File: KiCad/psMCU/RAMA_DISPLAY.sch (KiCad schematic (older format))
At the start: 7 parts

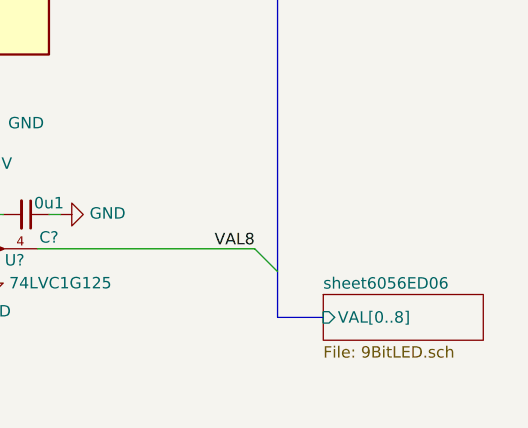
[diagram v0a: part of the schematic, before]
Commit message: Started ClockTest PCB
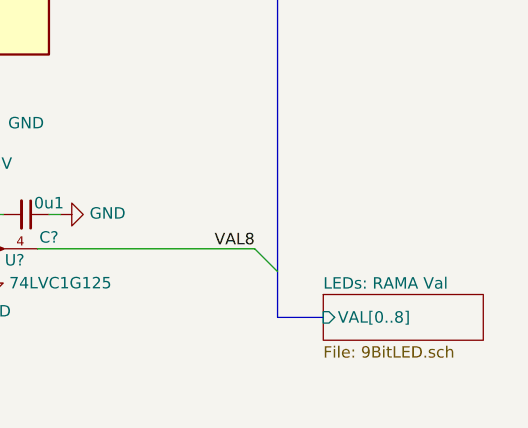
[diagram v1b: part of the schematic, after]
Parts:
- removed C?: 0u1, Capacitor_SMD:C_0603_1608Metric, symbol Device:C_Small
- removed R?: 10K, Resistor_SMD:R_0603_1608Metric, symbol Device:R_Small
- removed U?: 74HC245, symbol 74xx:74HC245
- removed U?: 74LVC1G04, Package_TO_SOT_SMD:SOT-353_SC-70-5, symbol 74xGxx:74LVC1G04
- added C?: 0u1, Capacitor_SMD:C_0603_1608Metric, symbol Device:C_Small
- added R?: 10K, Resistor_SMD:R_0603_1608Metric, symbol Device:R_Small
- added U?: 74HC245, symbol 74xx:74HC245
- added U?: 74LVC1G04, Package_TO_SOT_SMD:SOT-353_SC-70-5, symbol 74xGxx:74LVC1G04
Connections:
- net +5V: now also C?.2, U?.1 (A->B), U?.20 (VCC), U?.5 (VCC)
- net GND: now also C?.1, R?.2, U?.10 (GND), U?.3 (GND)
- net RAMA0: now also U?.2 (A0)
- net RAMA1: now also U?.3 (A1)
- net RAMA2: now also U?.4 (A2)
- net RAMA3: now also U?.5 (A3)
- net RAMA4: now also U?.6 (A4)
- net RAMA5: now also U?.7 (A5)
- net RAMA6: now also U?.8 (A6)
- net RAMA7: now also U?.9 (A7)
- net RAMA_OUT: now also R?.1, U?.2
- net VAL0: now also U?.18 (B0)
- net VAL1: now also U?.17 (B1)
- net VAL2: now also U?.16 (B2)
- net VAL3: now also U?.15 (B3)
- net VAL4: now also U?.14 (B4)
- net VAL5: now also U?.13 (B5)
- net VAL6: now also U?.12 (B6)
- net VAL7: now also U?.11 (B7)
- net at U?.1: now also U?.19 (CE), U?.4
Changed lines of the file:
@@
 $Descr A4 11693 8268
 encoding utf-8
-Sheet 79 94
-Title ""
+Sheet 77 193
+Title "psMCU"
 Date ""
 Rev ""
-Comp ""
+Comp "Philipp Schilk"
 Comment1 ""
 Comment2 ""
@@
 $Comp
 L 74xx:74HC245 U?
-U 1 1 5F40D07B
+U 1 1 5FDB352A
 P 5400 1900
-AR Path="/5ED2705B/5F40D07B" Ref="U?"  Part="1"
-AR Path="/5F1CE57C/5F40D07B" Ref="U?"  Part="1"
-AR Path="/5F396002/5F40D07B" Ref="U?"  Part="1"
-AR Path="/5F394B96/5F40D07B" Ref="U?"  Part="1"
-AR Path="/6041A022/5F40D07B" Ref="U?"  Part="1"
-AR Path="/604F08FB/5F40D07B" Ref="U?"  Part="1"
+AR Path="/5ED2705B/5FDB352A" Ref="U?"  Part="1"
+AR Path="/5F1CE57C/5FDB352A" Ref="U?"  Part="1"
+AR Path="/5F396002/5FDB352A" Ref="U?"  Part="1"
+AR Path="/5F394B96/5FDB352A" Ref="U?"  Part="1"
+AR Path="/6041A022/5FDB352A" Ref="U?"  Part="1"
+AR Path="/604F08FB/5FDB352A" Ref="U?"  Part="1"
 F 0 "U?" H 5500 2650 50  0000 C CNN
 F 1 "74HC245" H 5600 2550 50  0000 C CNN
@@
 $Comp
 L power:+5V #PWR?
-U 1 1 5F40D082
+U 1 1 5FDB352B
 P 5400 900
-AR Path="/5ED2705B/5F40D082" Ref="#PWR?"  Part="1"
-AR Path="/5F1CE57C/5F40D082" Ref="#PWR?"  Part="1"
-AR Path="/5F396002/5F40D082" Ref="#PWR?"  Part="1"
-AR Path="/5F394B96/5F40D082" Ref="#PWR?"  Part="1"
-AR Path="/6041A022/5F40D082" Ref="#PWR?"  Part="1"
-AR Path="/604F08FB/5F40D082" Ref="#PWR?"  Part="1"
+AR Path="/5ED2705B/5FDB352B" Ref="#PWR?"  Part="1"
+AR Path="/5F1CE57C/5FDB352B" Ref="#PWR?"  Part="1"
+AR Path="/5F396002/5FDB352B" Ref="#PWR?"  Part="1"
+AR Path="/5F394B96/5FDB352B" Ref="#PWR?"  Part="1"
+AR Path="/6041A022/5FDB352B" Ref="#PWR?"  Part="1"
+AR Path="/604F08FB/5FDB352B" Ref="#PWR?"  Part="1"
 F 0 "#PWR?" H 5400 750 50  0001 C CNN
 F 1 "+5V" H 5250 1000 50  0000 C CNN
@@
 $Comp
 L power:GND #PWR?
-U 1 1 5F40D091
+U 1 1 5FDB352D
 P 5700 1000
-AR Path="/5ED2705B/5F40D091" Ref="#PWR?"  Part="1"
-AR Path="/5F1CE57C/5F40D091" Ref="#PWR?"  Part="1"
-AR Path="/5F396002/5F40D091" Ref="#PWR?"  Part="1"
-AR Path="/5F394B96/5F40D091" Ref="#PWR?"  Part="1"
-AR Path="/6041A022/5F40D091" Ref="#PWR?"  Part="1"
-AR Path="/604F08FB/5F40D091" Ref="#PWR?"  Part="1"
+AR Path="/5ED2705B/5FDB352D" Ref="#PWR?"  Part="1"
+AR Path="/5F1CE57C/5FDB352D" Ref="#PWR?"  Part="1"
+AR Path="/5F396002/5FDB352D" Ref="#PWR?"  Part="1"
+AR Path="/5F394B96/5FDB352D" Ref="#PWR?"  Part="1"
+AR Path="/6041A022/5FDB352D" Ref="#PWR?"  Part="1"
+AR Path="/604F08FB/5FDB352D" Ref="#PWR?"  Part="1"
 F 0 "#PWR?" H 5700 750 50  0001 C CNN
 F 1 "GND" V 5705 872 50  0000 R CNN
@@
 $Comp
 L power:GND #PWR?
-U 1 1 5F40D098
+U 1 1 5FDB352E
 P 5400 2750
-AR Path="/5ED2705B/5F40D098" Ref="#PWR?"  Part="1"
-AR Path="/5F1CE57C/5F40D098" Ref="#PWR?"  Part="1"
-AR Path="/5F396002/5F40D098" Ref="#PWR?"  Part="1"
-AR Path="/5F394B96/5F40D098" Ref="#PWR?"  Part="1"
-AR Path="/6041A022/5F40D098" Ref="#PWR?"  Part="1"
-AR Path="/604F08FB/5F40D098" Ref="#PWR?"  Part="1"
+AR Path="/5ED2705B/5FDB352E" Ref="#PWR?"  Part="1"
+AR Path="/5F1CE57C/5FDB352E" Ref="#PWR?"  Part="1"
+AR Path="/5F396002/5FDB352E" Ref="#PWR?"  Part="1"
+AR Path="/5F394B96/5FDB352E" Ref="#PWR?"  Part="1"
+AR Path="/6041A022/5FDB352E" Ref="#PWR?"  Part="1"
+AR Path="/604F08FB/5FDB352E" Ref="#PWR?"  Part="1"
 F 0 "#PWR?" H 5400 2500 50  0001 C CNN
 F 1 "GND" H 5600 2700 50  0000 C CNN
@@
 $Sheet
 S 2650 3750 700  200
-U 5F41B94B
+U 5FDB3530
 F0 "LED: RAMA Active" 50
 F1 "1BitLED.sch" 50
@@
 $Comp
 L Device:R_Small R?
-U 1 1 5F3B0CCC
+U 1 1 5FDB3525
 P 2250 3200
-AR Path="/5F394B96/5F3B0CCC" Ref="R?"  Part="1"
-AR Path="/6041A022/5F3B0CCC" Ref="R?"  Part="1"
-AR Path="/604F08FB/5F3B0CCC" Ref="R?"  Part="1"
+AR Path="/5F394B96/5FDB3525" Ref="R?"  Part="1"
+AR Path="/6041A022/5FDB3525" Ref="R?"  Part="1"
+AR Path="/604F08FB/5FDB3525" Ref="R?"  Part="1"
 F 0 "R?" H 2309 3246 50  0000 L CNN
 F 1 "10K" H 2309 3155 50  0000 L CNN
@@
 $Comp
 L power:GND #PWR?
-U 1 1 5F3B869C
+U 1 1 5FDB3529
 P 3250 2850
-AR Path="/5ED2705B/5F3B869C" Ref="#PWR?"  Part="1"
-AR Path="/5F1CE57C/5F3B869C" Ref="#PWR?"  Part="1"
-AR Path="/5F394B96/5F3B869C" Ref="#PWR?"  Part="1"
-AR Path="/6041A022/5F3B869C" Ref="#PWR?"  Part="1"
-AR Path="/604F08FB/5F3B869C" Ref="#PWR?"  Part="1"
+AR Path="/5ED2705B/5FDB3529" Ref="#PWR?"  Part="1"
+AR Path="/5F1CE57C/5FDB3529" Ref="#PWR?"  Part="1"
+AR Path="/5F394B96/5FDB3529" Ref="#PWR?"  Part="1"
+AR Path="/6041A022/5FDB3529" Ref="#PWR?"  Part="1"
+AR Path="/604F08FB/5FDB3529" Ref="#PWR?"  Part="1"
 F 0 "#PWR?" H 3250 2600 50  0001 C CNN
 F 1 "GND" V 3255 2722 50  0000 R CNN
@@
 $Comp
 L Device:C_Small C?
-U 1 1 5F3B8693
+U 1 1 5FDB3528
 P 3100 2850
-AR Path="/5ED2705B/5F3B8693" Ref="C?"  Part="1"
-AR Path="/5F1CE57C/5F3B8693" Ref="C?"  Part="1"
-AR Path="/5F394B96/5F3B8693" Ref="C?"  Part="1"
-AR Path="/6041A022/5F3B8693" Ref="C?"  Part="1"
-AR Path="/604F08FB/5F3B8693" Ref="C?"  Part="1"
+AR Path="/5ED2705B/5FDB3528" Ref="C?"  Part="1"
+AR Path="/5F1CE57C/5FDB3528" Ref="C?"  Part="1"
+AR Path="/5F394B96/5FDB3528" Ref="C?"  Part="1"
+AR Path="/6041A022/5FDB3528" Ref="C?"  Part="1"
+AR Path="/604F08FB/5FDB3528" Ref="C?"  Part="1"
 F 0 "C?" V 3200 2950 50  0000 C CNN
 F 1 "0u1" V 3050 2950 50  0000 C CNN
@@
 $Comp
 L power:+5V #PWR?
-U 1 1 5F3B868D
+U 1 1 5FDB3527
 P 2950 2800
-AR Path="/5ED2705B/5F3B868D" Ref="#PWR?"  Part="1"
-AR Path="/5F1CE57C/5F3B868D" Ref="#PWR?"  Part="1"
-AR Path="/5F394B96/5F3B868D" Ref="#PWR?"  Part="1"
-AR Path="/6041A022/5F3B868D" Ref="#PWR?"  Part="1"
-AR Path="/604F08FB/5F3B868D" Ref="#PWR?"  Part="1"
+AR Path="/5ED2705B/5FDB3527" Ref="#PWR?"  Part="1"
+AR Path="/5F1CE57C/5FDB3527" Ref="#PWR?"  Part="1"
+AR Path="/5F394B96/5FDB3527" Ref="#PWR?"  Part="1"
+AR Path="/6041A022/5FDB3527" Ref="#PWR?"  Part="1"
+AR Path="/604F08FB/5FDB3527" Ref="#PWR?"  Part="1"
 F 0 "#PWR?" H 2950 2650 50  0001 C CNN
 F 1 "+5V" H 2965 2973 50  0000 C CNN
@@
 $Comp
 L 74xGxx:74LVC1G04 U?
-U 1 1 5F783D7F
+U 1 1 5FDB3531
 P 2950 3050
-AR Path="/5ED2705B/5F783D7F" Ref="U?"  Part="1"
-AR Path="/5F1CE57C/5F783D7F" Ref="U?"  Part="1"
-AR Path="/5F394B96/5F783D7F" Ref="U?"  Part="1"
-AR Path="/6041A022/5F783D7F" Ref="U?"  Part="1"
-AR Path="/604F08FB/5F783D7F" Ref="U?"  Part="1"
+AR Path="/5ED2705B/5FDB3531" Ref="U?"  Part="1"
+AR Path="/5F1CE57C/5FDB3531" Ref="U?"  Part="1"
+AR Path="/5F394B96/5FDB3531" Ref="U?"  Part="1"
+AR Path="/6041A022/5FDB3531" Ref="U?"  Part="1"
+AR Path="/604F08FB/5FDB3531" Ref="U?"  Part="1"
 F 0 "U?" H 3050 2850 50  0000 C CNN
 F 1 "74LVC1G04" H 3200 2950 50  0000 C CNN
@@
 S 6900 3550 700  200
 U 6056ED09
-F0 "sheet6056ED06" 50
+F0 "LEDs: RAMA Val" 50
 F1 "9BitLED.sch" 50
 F2 "VAL[0..8]" I L 6900 3650 50

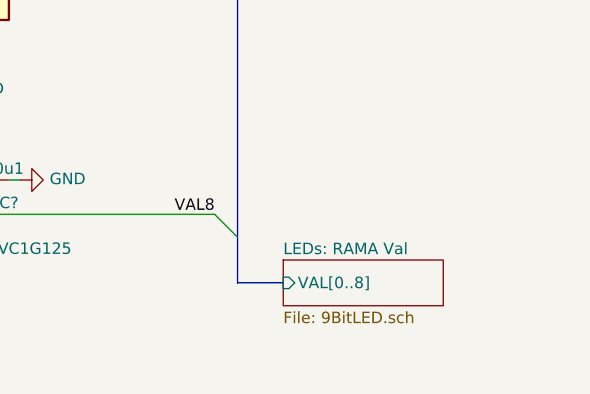
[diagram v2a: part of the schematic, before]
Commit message: First ERC pass
    All unconnects solved, need to inspect Tristate errors.
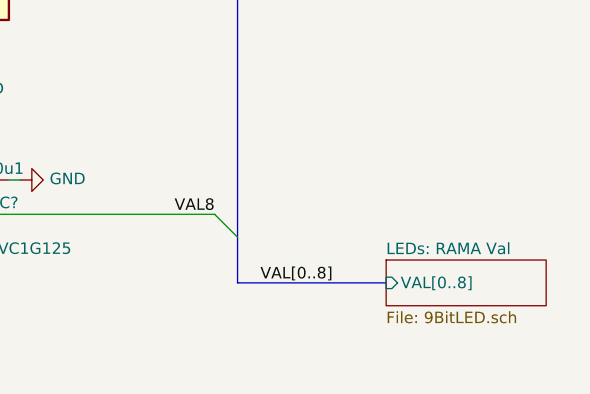
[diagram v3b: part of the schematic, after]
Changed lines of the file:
@@
 $Descr A4 11693 8268
 encoding utf-8
-Sheet 77 209
+Sheet 181 207
 Title "psMCU"
 Date ""
@@
 VAL8
 Wire Bus Line
-	6700 3650 6900 3650
+	6700 3650 7350 3650
 Wire Wire Line
 	5650 3350 6600 3350
@@
 RAMA8
 $Sheet
-S 6900 3550 700  200
+S 7350 3550 700  200
 U 6056ED09
 F0 "LEDs: RAMA Val" 50
 F1 "9BitLED.sch" 50
-F2 "VAL[0..8]" I L 6900 3650 50
+F2 "VAL[0..8]" I L 7350 3650 50
 $EndSheet
 Wire Bus Line
@@
 Wire Bus Line
 	6700 1500 6700 3650
+Text Label 6800 3650 0    50   ~ 0
+VAL[0..8]
 $EndSCHEMATC

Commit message: Added some footprints, small optimisations
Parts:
- U?: footprint (none) -> Package_SO:SSOP-20_5.3x7.2mm_P0.65mm
- U?: footprint (none) -> Package_TO_SOT_SMD:SOT-353_SC-70-5
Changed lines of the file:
@@
 F 0 "U?" H 5500 2650 50  0000 C CNN
 F 1 "74HC245" H 5600 2550 50  0000 C CNN
-F 2 "" H 5400 1900 50  0001 C CNN
+F 2 "Package_SO:SSOP-20_5.3x7.2mm_P0.65mm" H 5400 1900 50  0001 C CNN
 F 3 "http://www.ti.com/lit/gpn/sn74HC245" H 5400 1900 50  0001 C CNN
 	1    5400 1900
@@
 F 0 "U?" H 5550 3300 50  0000 C CNN
 F 1 "74LVC1G125" H 5750 3200 50  0000 C CNN
-F 2 "" H 5400 3350 50  0001 C CNN
+F 2 "Package_TO_SOT_SMD:SOT-353_SC-70-5" H 5400 3350 50  0001 C CNN
 F 3 "http://www.ti.com/lit/sg/scyt129e/scyt129e.pdf" H 5400 3350 50  0001 C CNN
 	1    5400 3350

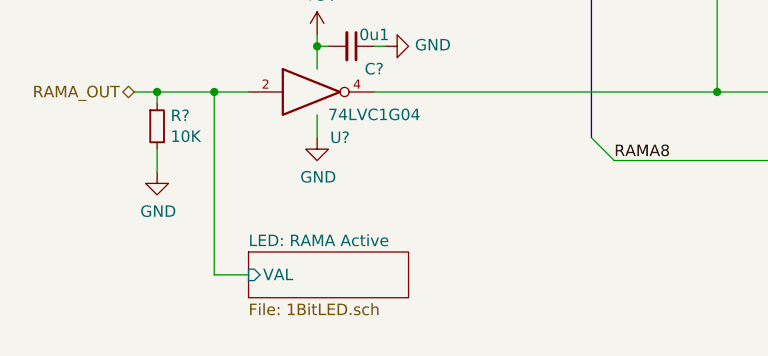
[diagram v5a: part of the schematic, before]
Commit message: Removed Single LED sheets
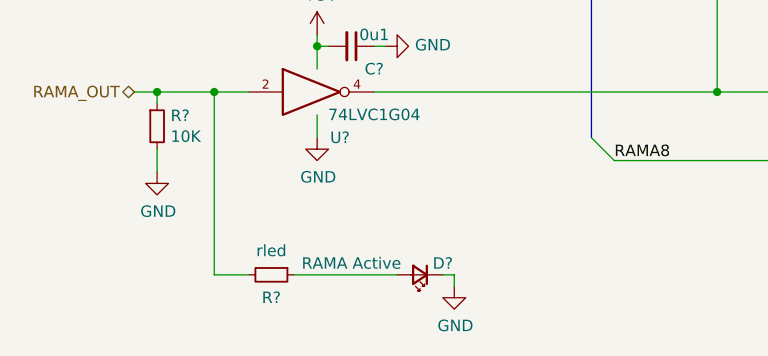
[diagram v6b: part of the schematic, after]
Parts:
- added D?: RAMA Active, Diode_SMD:D_0603_1608Metric, symbol Device:LED_Small
- added R?: rled, Resistor_SMD:R_0603_1608Metric, symbol Device:R_Small
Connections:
- net GND: now also D?.1 (K)
- net RAMA_OUT: now also R?.2
- new net: D?.2 (A), R?.1

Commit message: First Schematic Draft done.
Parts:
- added R412: 10K, symbol Device:R_Small
- added RN13, RN14: 10K, Resistor_SMD:R_Array_Convex_4x0603, symbol Device:R_Pack04
- C364, C365, C366: renamed from C?; footprint Capacitor_SMD:C_0603_1608Metric -> NoRef_Footprints:C_0603_1608Metric_NoRef
- D380: renamed from D?; footprint Diode_SMD:D_0603_1608Metric -> NoRef_Footprints:D_0603_1608Metric_NoRef
- R410: renamed from R?; footprint Resistor_SMD:R_0603_1608Metric -> NoRef_Footprints:D_0603_1608Metric_NoRef
- R411: renamed from R?; footprint Resistor_SMD:R_0603_1608Metric -> NoRef_Footprints:R_0603_1608Metric
- gave numbers to parts that had none: 3
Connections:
- net GND: now also R412.1, RN13.5 (R4.2), RN13.6 (R3.2), RN13.7 (R2.2), RN13.8 (R1.2), RN14.5 (R4.2), RN14.6 (R3.2), RN14.7 (R2.2), RN14.8 (R1.2)
- net RAMA0: now also RN13.1 (R1.1)
- net RAMA1: now also RN13.2 (R2.1)
- net RAMA2: now also RN13.3 (R3.1)
- net RAMA3: now also RN13.4 (R4.1)
- net RAMA4: now also RN14.1 (R1.1)
- net RAMA5: now also RN14.2 (R2.1)
- net RAMA6: now also RN14.3 (R3.1)
- net RAMA7: now also RN14.4 (R4.1)
- net RAMA8: now also R412.2
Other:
- moved on the sheet: C364, C365, C366, D380, R410, R411, U348, U349, U350

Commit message: Small improvements.
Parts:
- renumbered C364 to C362, C365 to C363, C366 to C364, U348 to U346, U349 to U347, U350 to U348
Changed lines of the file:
@@
 AR Path="/5F394B96/5FDB352B" Ref="#PWR?"  Part="1"
 AR Path="/6041A022/5FDB352B" Ref="#PWR?"  Part="1"
-AR Path="/604F08FB/5FDB352B" Ref="#PWR01536"  Part="1"
-F 0 "#PWR01536" H 7300 2300 50  0001 C CNN
+AR Path="/604F08FB/5FDB352B" Ref="#PWR01521"  Part="1"
+F 0 "#PWR01521" H 7300 2300 50  0001 C CNN
 F 1 "+5V" H 7150 2550 50  0000 C CNN
 F 2 "" H 7300 2450 50  0001 C CNN
@@
 AR Path="/5F394B96/5F40D088" Ref="C?"  Part="1"
 AR Path="/6041A022/5F40D088" Ref="C?"  Part="1"
-AR Path="/604F08FB/5F40D088" Ref="C365"  Part="1"
-F 0 "C365" V 7221 2550 50  0000 C CNN
+AR Path="/604F08FB/5F40D088" Ref="C363"  Part="1"
+F 0 "C363" V 7221 2550 50  0000 C CNN
 F 1 "0u1" V 7312 2550 50  0000 C CNN
 F 2 "NoRef_Footprints:C_0603_1608Metric_NoRef" H 7450 2550 50  0001 C CNN
@@
 AR Path="/5F394B96/5FDB352D" Ref="#PWR?"  Part="1"
 AR Path="/6041A022/5FDB352D" Ref="#PWR?"  Part="1"
-AR Path="/604F08FB/5FDB352D" Ref="#PWR01540"  Part="1"
-F 0 "#PWR01540" H 7600 2300 50  0001 C CNN
+AR Path="/604F08FB/5FDB352D" Ref="#PWR01525"  Part="1"
+F 0 "#PWR01525" H 7600 2300 50  0001 C CNN
 F 1 "GND" V 7605 2422 50  0000 R CNN
 F 2 "" H 7600 2550 50  0001 C CNN
@@
 AR Path="/5F394B96/5FDB352E" Ref="#PWR?"  Part="1"
 AR Path="/6041A022/5FDB352E" Ref="#PWR?"  Part="1"
-AR Path="/604F08FB/5FDB352E" Ref="#PWR01537"  Part="1"
-F 0 "#PWR01537" H 7300 4050 50  0001 C CNN
+AR Path="/604F08FB/5FDB352E" Ref="#PWR01522"  Part="1"
+F 0 "#PWR01522" H 7300 4050 50  0001 C CNN
 F 1 "GND" H 7500 4250 50  0000 C CNN
 F 2 "" H 7300 4300 50  0001 C CNN
@@
 AR Path="/5F394B96/5F415EC0" Ref="#PWR?"  Part="1"
 AR Path="/6041A022/5F415EC0" Ref="#PWR?"  Part="1"
-AR Path="/604F08FB/5F415EC0" Ref="#PWR01535"  Part="1"
-F 0 "#PWR01535" H 6750 3700 50  0001 C CNN
+AR Path="/604F08FB/5F415EC0" Ref="#PWR01520"  Part="1"
+F 0 "#PWR01520" H 6750 3700 50  0001 C CNN
 F 1 "+5V" V 6750 4050 50  0000 C CNN
 F 2 "" H 6750 3850 50  0001 C CNN
@@
 AR Path="/5F394B96/5F783D83" Ref="#PWR?"  Part="1"
 AR Path="/6041A022/5F783D83" Ref="#PWR?"  Part="1"
-AR Path="/604F08FB/5F783D83" Ref="#PWR01530"  Part="1"
-F 0 "#PWR01530" H 3500 4550 50  0001 C CNN
+AR Path="/604F08FB/5F783D83" Ref="#PWR01515"  Part="1"
+F 0 "#PWR01515" H 3500 4550 50  0001 C CNN
 F 1 "GND" H 3505 4627 50  0000 C CNN
 F 2 "" H 3500 4800 50  0001 C CNN
@@
 AR Path="/5F394B96/5FDB3529" Ref="#PWR?"  Part="1"
 AR Path="/6041A022/5FDB3529" Ref="#PWR?"  Part="1"
-AR Path="/604F08FB/5FDB3529" Ref="#PWR01531"  Part="1"
-F 0 "#PWR01531" H 3800 4150 50  0001 C CNN
+AR Path="/604F08FB/5FDB3529" Ref="#PWR01516"  Part="1"
+F 0 "#PWR01516" H 3800 4150 50  0001 C CNN
 F 1 "GND" V 3805 4272 50  0000 R CNN
 F 2 "" H 3800 4400 50  0001 C CNN
@@
 AR Path="/5F394B96/5FDB3528" Ref="C?"  Part="1"
 AR Path="/6041A022/5FDB3528" Ref="C?"  Part="1"
-AR Path="/604F08FB/5FDB3528" Ref="C364"  Part="1"
-F 0 "C364" V 3750 4500 50  0000 C CNN
+AR Path="/604F08FB/5FDB3528" Ref="C362"  Part="1"
+F 0 "C362" V 3750 4500 50  0000 C CNN
 F 1 "0u1" V 3600 4500 50  0000 C CNN
 F 2 "NoRef_Footprints:C_0603_1608Metric_NoRef" H 3650 4400 50  0001 C CNN
@@
 AR Path="/5F394B96/5FDB3527" Ref="#PWR?"  Part="1"
 AR Path="/6041A022/5FDB3527" Ref="#PWR?"  Part="1"
-AR Path="/604F08FB/5FDB3527" Ref="#PWR01529"  Part="1"
-F 0 "#PWR01529" H 3500 4200 50  0001 C CNN
+AR Path="/604F08FB/5FDB3527" Ref="#PWR01514"  Part="1"
+F 0 "#PWR01514" H 3500 4200 50  0001 C CNN
 F 1 "+5V" H 3515 4523 50  0000 C CNN
 F 2 "" H 3500 4350 50  0001 C CNN
@@
 AR Path="/5F394B96/5FDB3531" Ref="U?"  Part="1"
 AR Path="/6041A022/5FDB3531" Ref="U?"  Part="1"
-AR Path="/604F08FB/5FDB3531" Ref="U348"  Part="1"
-F 0 "U348" H 3600 4400 50  0000 C CNN
+AR Path="/604F08FB/5FDB3531" Ref="U346"  Part="1"
+F 0 "U346" H 3600 4400 50  0000 C CNN
 F 1 "74LVC1G04" H 3750 4500 50  0000 C CNN
 F 2 "Package_TO_SOT_SMD:SOT-353_SC-70-5" H 3500 4600 50  0001 C CNN
@@
 AR Path="/5F394B96/5F3B281D" Ref="#PWR?"  Part="1"
 AR Path="/6041A022/5F3B281D" Ref="#PWR?"  Part="1"
-AR Path="/604F08FB/5F3B281D" Ref="#PWR01528"  Part="1"
-F 0 "#PWR01528" H 2800 4700 50  0001 C CNN
+AR Path="/604F08FB/5F3B281D" Ref="#PWR01513"  Part="1"
+F 0 "#PWR01513" H 2800 4700 50  0001 C CNN
 F 1 "GND" H 2805 4777 50  0000 C CNN
 F 2 "" H 2800 4950 50  0001 C CNN
@@
 AR Path="/5F1CE57C/6052A2A2" Ref="#PWR?"  Part="1"
 AR Path="/5F396002/6052A2A2" Ref="#PWR?"  Part="1"
-AR Path="/604F08FB/6052A2A2" Ref="#PWR01539"  Part="1"
-F 0 "#PWR01539" H 7350 4750 50  0001 C CNN
+AR Path="/604F08FB/6052A2A2" Ref="#PWR01524"  Part="1"
+F 0 "#PWR01524" H 7350 4750 50  0001 C CNN
 F 1 "GND" H 7355 4827 50  0000 C CNN
 F 2 "" H 7350 5000 50  0001 C CNN
@@
 AR Path="/5F1CE57C/6052A2A9" Ref="#PWR?"  Part="1"
 AR Path="/5F396002/6052A2A9" Ref="#PWR?"  Part="1"
-AR Path="/604F08FB/6052A2A9" Ref="#PWR01541"  Part="1"
-F 0 "#PWR01541" H 7650 4500 50  0001 C CNN
+AR Path="/604F08FB/6052A2A9" Ref="#PWR01526"  Part="1"
+F 0 "#PWR01526" H 7650 4500 50  0001 C CNN
 F 1 "GND" V 7655 4622 50  0000 R CNN
 F 2 "" H 7650 4750 50  0001 C CNN
@@
 AR Path="/5F1CE57C/6052A2B2" Ref="C?"  Part="1"
 AR Path="/5F396002/6052A2B2" Ref="C?"  Part="1"
-AR Path="/604F08FB/6052A2B2" Ref="C366"  Part="1"
-F 0 "C366" V 7600 4850 50  0000 C CNN
+AR Path="/604F08FB/6052A2B2" Ref="C364"  Part="1"
+F 0 "C364" V 7600 4850 50  0000 C CNN
 F 1 "0u1" V 7450 4850 50  0000 C CNN
 F 2 "NoRef_Footprints:C_0603_1608Metric_NoRef" H 7500 4750 50  0001 C CNN
@@
 AR Path="/5F1CE57C/6052A2B8" Ref="#PWR?"  Part="1"
 AR Path="/5F396002/6052A2B8" Ref="#PWR?"  Part="1"
-AR Path="/604F08FB/6052A2B8" Ref="#PWR01538"  Part="1"
-F 0 "#PWR01538" H 7350 4550 50  0001 C CNN
+AR Path="/604F08FB/6052A2B8" Ref="#PWR01523"  Part="1"
+F 0 "#PWR01523" H 7350 4550 50  0001 C CNN
 F 1 "+5V" H 7365 4873 50  0000 C CNN
 F 2 "" H 7350 4700 50  0001 C CNN
@@
 AR Path="/5F1CE57C/6052A2BF" Ref="U?"  Part="1"
 AR Path="/5F396002/6052A2BF" Ref="U?"  Part="1"
-AR Path="/604F08FB/6052A2BF" Ref="U350"  Part="1"
-F 0 "U350" H 7450 4850 50  0000 C CNN
+AR Path="/604F08FB/6052A2BF" Ref="U348"  Part="1"
+F 0 "U348" H 7450 4850 50  0000 C CNN
 F 1 "74LVC1G125" H 7650 4750 50  0000 C CNN
 F 2 "Package_TO_SOT_SMD:SOT-353_SC-70-5" H 7300 4900 50  0001 C CNN
@@
 AR Path="/5F18F3CA/62BFBAAA" Ref="#PWR?"  Part="1"
 AR Path="/60E33DBC/5FD12DEC/62BFBAAA" Ref="#PWR?"  Part="1"
-AR Path="/604F08FB/62BFBAAA" Ref="#PWR01532"  Part="1"
-F 0 "#PWR01532" H 4100 5200 50  0001 C CNN
+AR Path="/604F08FB/62BFBAAA" Ref="#PWR01517"  Part="1"
+F 0 "#PWR01517" H 4100 5200 50  0001 C CNN
 F 1 "GND" H 4105 5277 50  0000 C CNN
 F 2 "" H 4100 5450 50  0001 C CNN
@@
 AR Path="/5F394B96/6061F332" Ref="#PWR?"  Part="1"
 AR Path="/6041A022/6061F332" Ref="#PWR?"  Part="1"
-AR Path="/604F08FB/6061F332" Ref="#PWR01533"  Part="1"
-F 0 "#PWR01533" H 6100 5050 50  0001 C CNN
+AR Path="/604F08FB/6061F332" Ref="#PWR01518"  Part="1"
+F 0 "#PWR01518" H 6100 5050 50  0001 C CNN
 F 1 "GND" V 6105 5172 50  0000 R CNN
 F 2 "" H 6100 5300 50  0001 C CNN
@@
 AR Path="/5F394B96/5FDB352A" Ref="U?"  Part="1"
 AR Path="/6041A022/5FDB352A" Ref="U?"  Part="1"
-AR Path="/604F08FB/5FDB352A" Ref="U349"  Part="1"
-F 0 "U349" H 7400 4200 50  0000 C CNN
+AR Path="/604F08FB/5FDB352A" Ref="U347"  Part="1"
+F 0 "U347" H 7400 4200 50  0000 C CNN
 F 1 "74HC245" H 7500 4100 50  0000 C CNN
 F 2 "Package_SO:SSOP-20_5.3x7.2mm_P0.65mm" H 7300 3450 50  0001 C CNN
@@
 AR Path="/5F394B96/6059010B" Ref="#PWR?"  Part="1"
 AR Path="/6041A022/6059010B" Ref="#PWR?"  Part="1"
-AR Path="/604F08FB/6059010B" Ref="#PWR01534"  Part="1"
-F 0 "#PWR01534" H 6550 2100 50  0001 C CNN
+AR Path="/604F08FB/6059010B" Ref="#PWR01519"  Part="1"
+F 0 "#PWR01519" H 6550 2100 50  0001 C CNN
 F 1 "GND" V 6555 2222 50  0000 R CNN
 F 2 "" H 6550 2350 50  0001 C CNN
